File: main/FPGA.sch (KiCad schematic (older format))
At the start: 42 parts, among them J10 FPGA_GPIO, J3 FPGA_debug, U2 S25FL127S, U3 XC7A100T-FTG256, X1 20MHz Oscillator

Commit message: Some tweaks
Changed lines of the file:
@@
 encoding utf-8
 Sheet 7 7
-Title "Audio project FPGA connections"
-Date ""
-Rev "V01"
+Title "MIDI Audio Box"
+Date "2021-09-21"
+Rev "v01"
 Comp ""
 Comment1 ""
 Comment2 ""
-Comment3 ""
-Comment4 "Authors: Halvor Bjørstad, Iver Håkonsen"
+Comment3 "Authors: Iver Håkonsen, Halvor Bjørstad"
+Comment4 "TDT4295 Computer Design Project"
 $EndDescr
-Entry Wire Line
-	7600 9150 7700 9250
-Entry Wire Line
-	7600 9000 7700 9100
-Entry Wire Line
-	7600 8850 7700 8950
-Entry Wire Line
-	7600 8700 7700 8800
-Text Label 7600 8500 0    50   ~ 0
-MCU_SPI[0..3]
-Text Label 7700 8800 0    50   ~ 0
-MCU_SPI0
-Text Label 7700 8950 0    50   ~ 0
-MCU_SPI1
-Text Label 7700 9100 0    50   ~ 0
-MCU_SPI2
-Text Label 7700 9250 0    50   ~ 0
-MCU_SPI3
 Entry Wire Line
 	11100 3150 11200 3050
@@
 Text HLabel 10950 3950 0    50   Output ~ 0
 I2S[0..2]
-Wire Bus Line
-	7600 8450 7450 8450
-Text HLabel 7450 8450 0    50   BiDi ~ 0
-MCU_SPI[0..3]
 Wire Wire Line
 	5300 6000 5300 6100
@@
 NoConn ~ 15900 1750
 NoConn ~ 15900 2050
-Text Label 8350 8800 0    50   ~ 0
-MCU_SPI_CLK
-Text Label 8350 8950 0    50   ~ 0
-MCU_SPI_MOSI
-Text Label 8350 9100 0    50   ~ 0
-MCU_SPI_MISO
-Text Label 8350 9250 0    50   ~ 0
-MSU_SPI_CS
 Wire Wire Line
 	13100 7500 12800 7500
@@
 	11900 4350 9300 4350
 Wire Wire Line
-	9300 4350 9300 8800
-Wire Wire Line
-	7700 8800 9300 8800
-Wire Wire Line
 	11900 4950 9450 4950
 Wire Wire Line
-	9450 4950 9450 8950
-Wire Wire Line
-	7700 8950 9450 8950
-Wire Wire Line
-	9600 9100 9600 5050
-Wire Wire Line
 	9600 5050 11900 5050
 Wire Wire Line
-	7700 9100 9600 9100
-Wire Wire Line
 	11900 5150 9750 5150
-Wire Wire Line
-	9750 5150 9750 9250
-Wire Wire Line
-	7700 9250 9750 9250
 Wire Wire Line
 	11200 3050 11900 3050
@@
 Text Label 11450 5650 0    50   ~ 0
 GPIO9
+Wire Wire Line
+	7700 9900 9750 9900
+Wire Wire Line
+	7700 9750 9600 9750
+Wire Wire Line
+	7700 9600 9450 9600
+Wire Wire Line
+	7700 9450 9300 9450
+Text Label 8350 9900 0    50   ~ 0
+MSU_SPI_CS
+Text Label 8350 9750 0    50   ~ 0
+MCU_SPI_MISO
+Text Label 8350 9600 0    50   ~ 0
+MCU_SPI_MOSI
+Text Label 8350 9450 0    50   ~ 0
+MCU_SPI_CLK
+Text HLabel 7450 9100 0    50   BiDi ~ 0
+MCU_SPI[0..3]
+Wire Bus Line
+	7600 9100 7450 9100
+Text Label 7700 9900 0    50   ~ 0
+MCU_SPI3
+Text Label 7700 9750 0    50   ~ 0
+MCU_SPI2
+Text Label 7700 9600 0    50   ~ 0
+MCU_SPI1
+Text Label 7700 9450 0    50   ~ 0
+MCU_SPI0
+Text Label 7600 9150 0    50   ~ 0
+MCU_SPI[0..3]
+Entry Wire Line
+	7600 9350 7700 9450
+Entry Wire Line
+	7600 9500 7700 9600
+Entry Wire Line
+	7600 9650 7700 9750
+Entry Wire Line
+	7600 9800 7700 9900
+Wire Wire Line
+	9300 4350 9300 9450
+Wire Wire Line
+	9450 4950 9450 9600
+Wire Wire Line
+	9600 5050 9600 9750
+Wire Wire Line
+	9750 5150 9750 9900
 Wire Bus Line
 	11100 3150 11100 3950
 Wire Bus Line
-	7600 8450 7600 9150
+	7600 9100 7600 9800
 Wire Bus Line
 	12700 7350 12700 8050

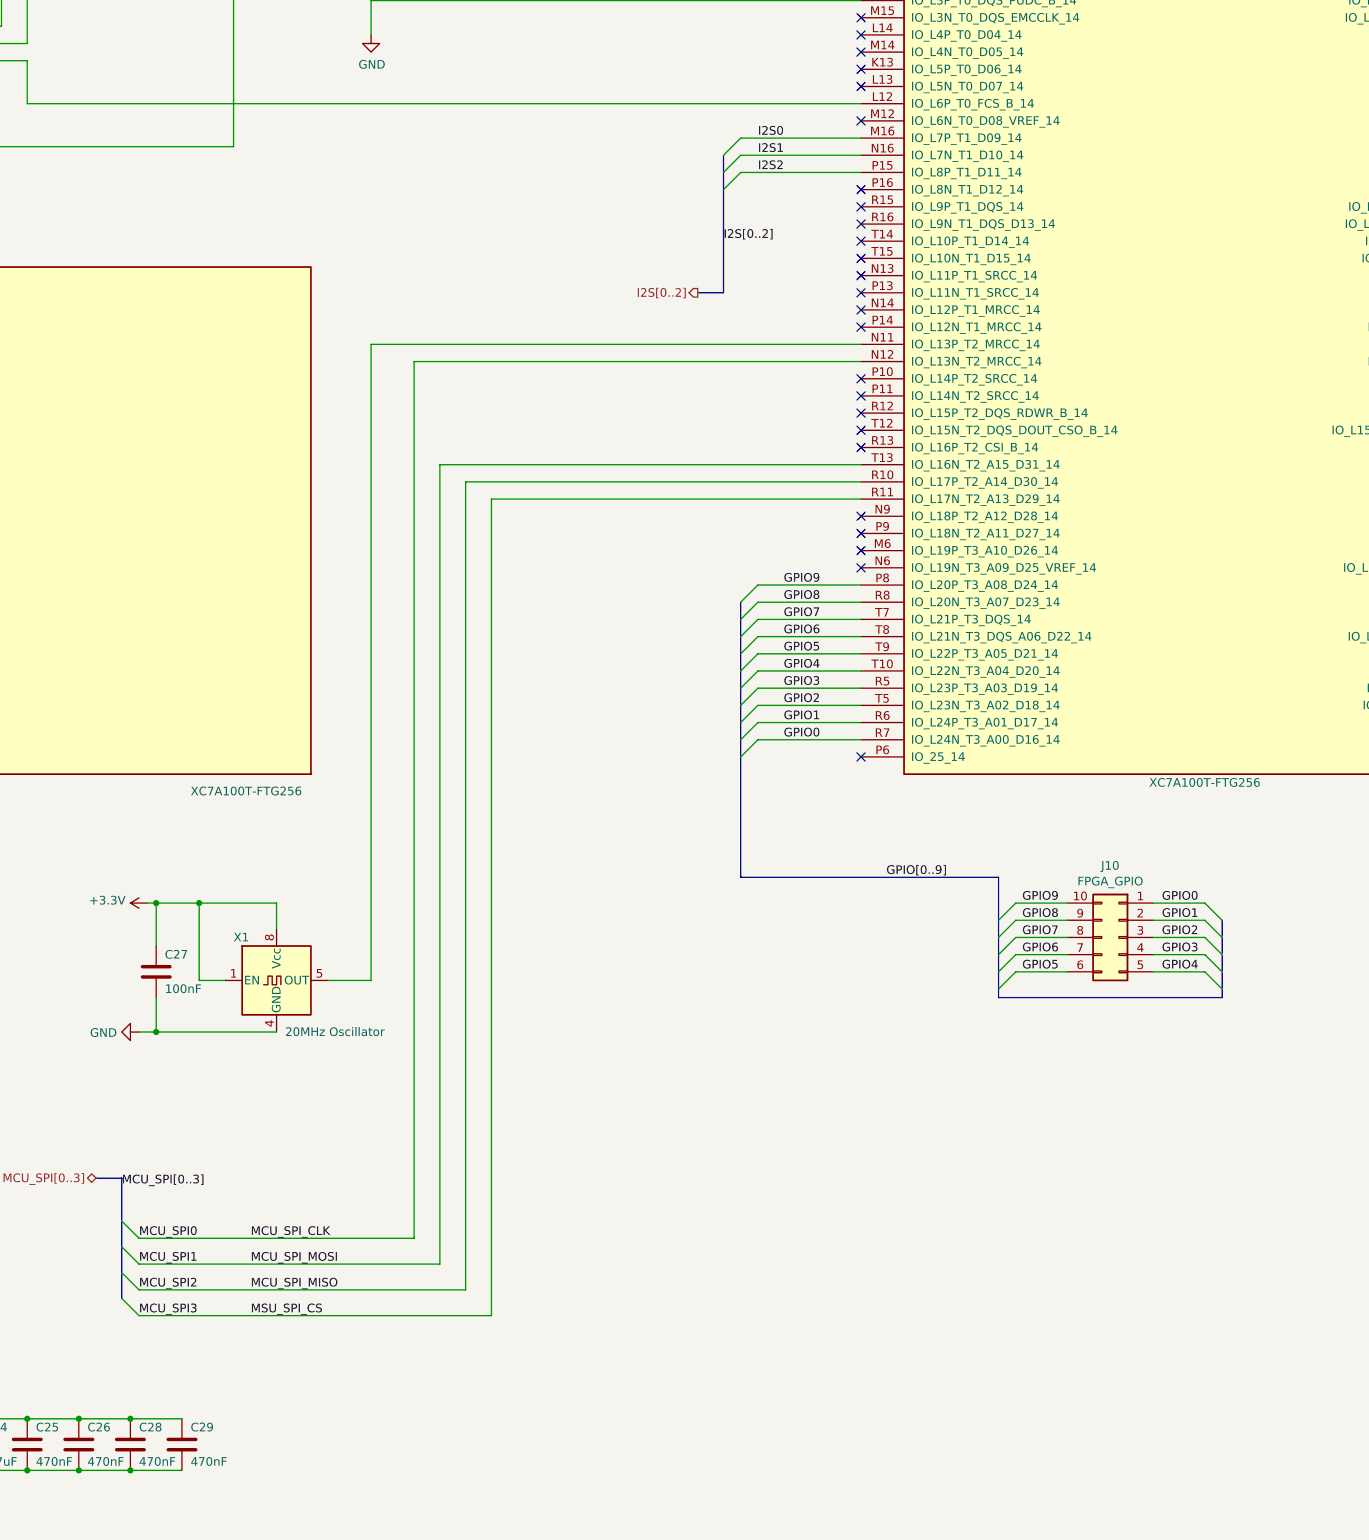
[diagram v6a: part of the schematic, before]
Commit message: Add FPGA RAM chip
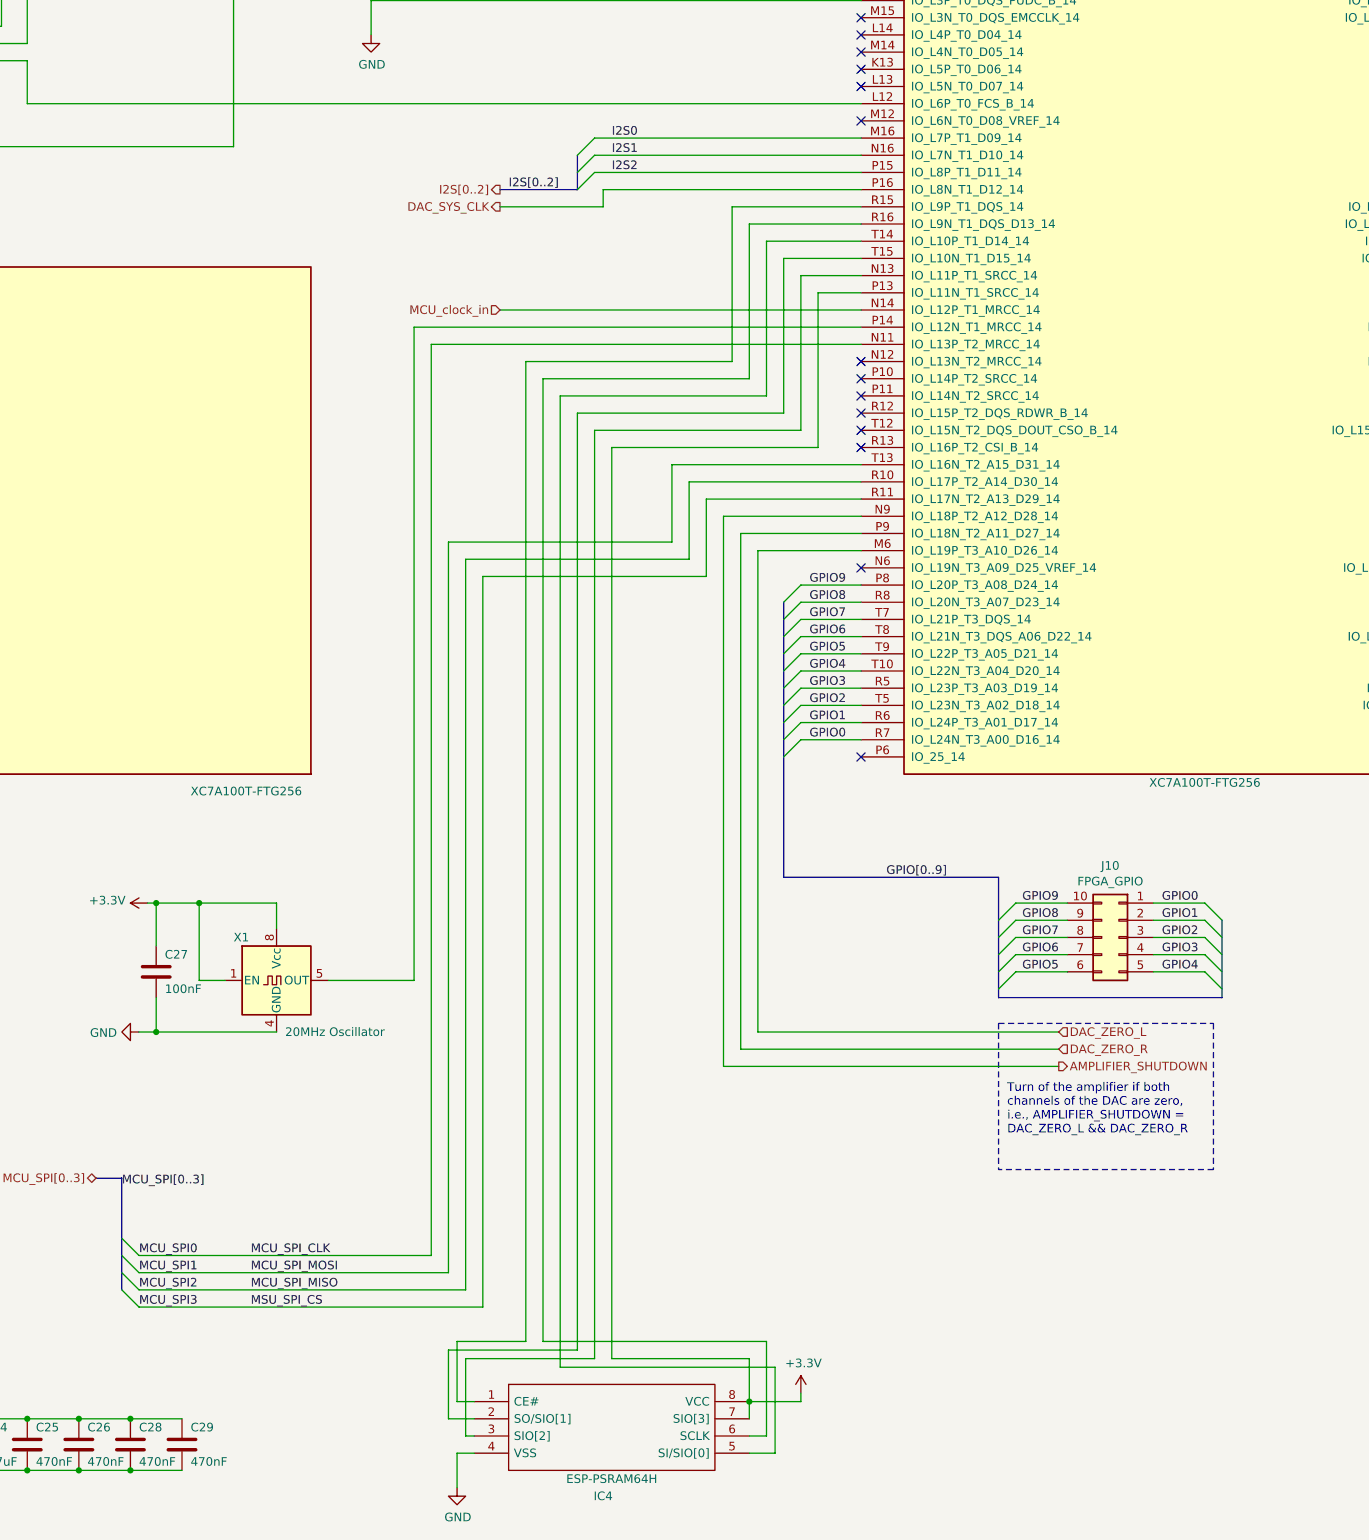
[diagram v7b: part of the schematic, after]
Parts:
- added IC4: ESP-PSRAM64H, SOIC127P600X175-8N, symbol ESP-PSRAM64H:ESP-PSRAM64H
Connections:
- net +3V3: now also U3.P13 (IO_L11N_T1_SRCC_14), IC4.7 (SIO[3]), IC4.8 (VCC)
- net GND: now also IC4.4 (VSS)
- net MCU_SPI0: now also U3.N11 (IO_L13P_T2_MRCC_14); no longer U3.N12 (IO_L13N_T2_MRCC_14)
- net DAC_ZERO_L: now reaches U3.M6 (IO_L19P_T3_A10_D26_14)
- net at X1.5 (OUT): now also U3.P14 (IO_L12N_T1_MRCC_14); no longer U3.N11 (IO_L13P_T2_MRCC_14)
- net at U3.N13 (IO_L11P_T1_SRCC_14): now also IC4.3 (SIO[2])
- net MCU_clock_in: now reaches U3.N14 (IO_L12P_T1_MRCC_14)
- net AMPLIFIER_SHUTDOWN: now reaches U3.N9 (IO_L18P_T2_A12_D28_14)
- net DAC_SYS_CLK: now reaches U3.P16 (IO_L8N_T1_D12_14)
- net DAC_ZERO_R: now reaches U3.P9 (IO_L18N_T2_A11_D27_14)
- net at U3.R15 (IO_L9P_T1_DQS_14): now also IC4.1 (CE#)
- net at U3.R16 (IO_L9N_T1_DQS_D13_14): now also IC4.6 (SCLK)
- net at U3.T14 (IO_L10P_T1_D14_14): now also IC4.5 (SI/SIO[0])
- net at U3.T15 (IO_L10N_T1_D15_14): now also IC4.2 (SO/SIO[1])
- no-connect marks 80 -> 69
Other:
- note added: "Turn of the amplifier if both\nchannels of the DAC are zero,\ni.e., AMPLIFIER_SHUTDOWN = \nDAC_ZERO_L && DAC_ZERO_R"

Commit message: Final cleanup before sending in for rebiew
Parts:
- added C56: 470nF, symbol Device:C
- renumbered C1 to C27, C2 to C28, C3 to C29, C4 to C30, C5 to C31, C6 to C32, C7 to C33, C8 to C34, C9 to C35, C10 to C36, C11 to C37, C12 to C38, C13 to C39, C14 to C40, C15 to C41, C16 to C42, C17 to C43, C18 to C44, C19 to C45, C20 to C46, C21 to C47, C22 to C48, C23 to C49, C24 to C50, C25 to C51, C26 to C52, C28 to C53, C27 to C54, C29 to C55, J3 to J8, J10 to J9, R6 to R32, R7 to R33, R8 to R34, R9 to R35, R10 to R36, R11 to R37, R12 to R38, R13 to R39, U2 to U4
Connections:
- net +3V3: now also C56.1
- net GND: now also C56.2
